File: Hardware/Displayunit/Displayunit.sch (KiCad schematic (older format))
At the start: 142 parts, among them IC1 TSC2007, IC2 MX25LM51245GXDI00, IC3 IS66WVH8M8BLL-100B1LI_0, IC4 TPS61165DRVR, J1 615008138221, J10 ER-CON10HT-1, J2 615008138221, J3 54104-4031, J4 Conn_ARM_JTAG_SWD_20, J5 52271-0679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

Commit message: Display Unit Zusätzliche Buchsen Mini Fit für den Bus, Befestigung um 5mm verschoben, Bauteil Placement.
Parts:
- removed C52: 5n6, Capacitor_SMD:C_0603_1608Metric, symbol Displayunit-rescue:C-Device
- removed J7: WAGO_Klemmleiste_2-pol, WAGO:WAGO_Klemmleiste_Hebel4mm²Horizontal_RM5mm_2-pol, symbol WAGO:WAGO_Klemmleiste_2-pol
- removed U6: SN65HVD231DR, Package_SO:SOIC-8_3.9x4.9mm_P1.27mm, symbol Interface_CAN_LIN:SN65HVD231
- added J11, J7: Conn_02x03_Row_Letter_First, Connector_Molex:Molex_Micro-Fit_3.0_43045-0612_2x03_P3.00mm_Vertical, symbol Connector_Generic:Conn_02x03_Row_Letter_First
- added R27, R28: 4k7, Resistor_SMD:R_0603_1608Metric, symbol Displayunit-rescue:R-Device
- added SW3, SW4: SW_DIP_x01, Button_Switch_SMD:SW_SPST_CK_RS282G05A3, symbol Switch:SW_DIP_x01
- added U6: SN65HVD234, Package_SO:SOIC-8_3.9x4.9mm_P1.27mm, symbol Interface_CAN_LIN:SN65HVD234
- R18: value 60R -> 120R
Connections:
- net +3V3: now also U6.3 (VCC)
- net CAN_STB: now also U6.8 (Rs)
- net GND: now also J11.b1 (Pin_b1), J7.b1 (Pin_b1), R27.2, R28.2, U6.2 (GND)
- net I2C2_SCL: now also R27.1
- net I2C2_SDA: now also R28.1
- net VrefCAN: no longer R18.2, R19.1
- net at D5.1 (A1), FB4.2: now also SW4.2, U6.6 (CANL); no longer R19.2
- net at D5.2 (A2), FB3.2, R18.1: now also U6.7 (CANH)
- net at R23.1, R6.1: now also U6.1 (D)
- net at R24.1, R25.1: now also U6.4 (R)
- net Control+2: now reaches C53.1, D2.2 (A)
- net Control+2: now also J11.a1 (Pin_a1), J7.a1 (Pin_a1)
- net CAN_EN: now reaches U1.72 (PB15)
- net CAN_EN: now also U6.5 (EN)
- net at FB12.1, J1.3, J2.3: now also J11.a2 (Pin_a2), J7.a2 (Pin_a2)
- net at FB3.1, J1.4, J2.4: now also J11.b2 (Pin_b2), J7.b2 (Pin_b2)
- net at FB4.1, J1.5, J2.5: now also J11.b3 (Pin_b3), J7.b3 (Pin_b3)
- net at FB11.1, J1.6, J2.6: now also J11.a3 (Pin_a3), J7.a3 (Pin_a3)
- net at D8.1 (A1), FB12.2, U3.6 (A): now also SW3.2; no longer R26.2
- new net: R18.2, SW4.1
- new net: R26.2, SW3.1
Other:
- moved on the sheet: J6, R18, R19, R23, R24, R25, R26, R6

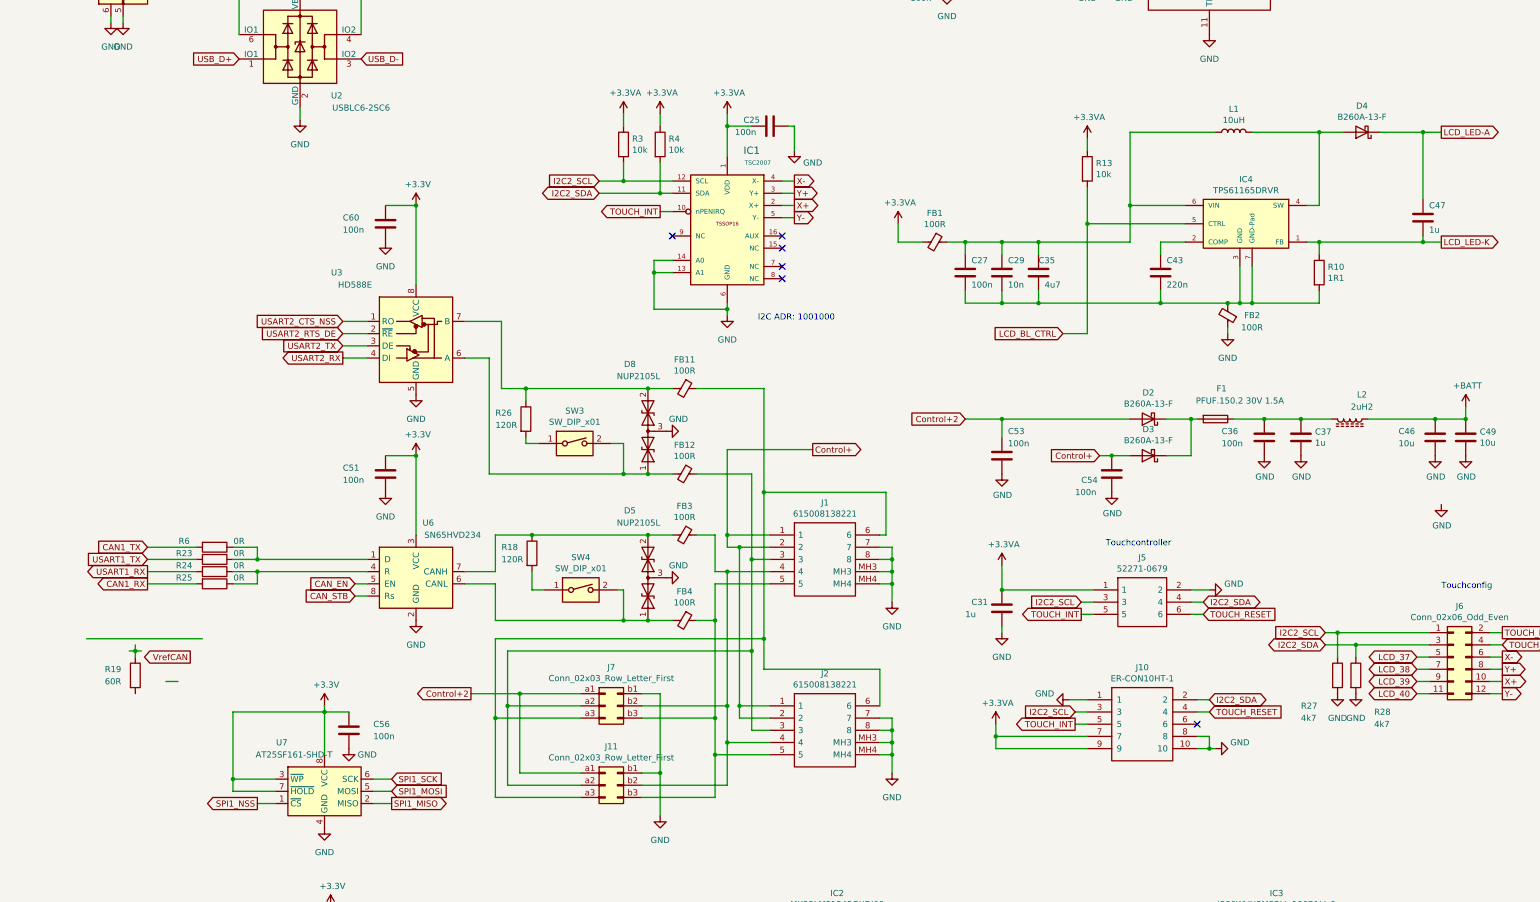
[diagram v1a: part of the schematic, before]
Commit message: Fehlende Teile gerouted
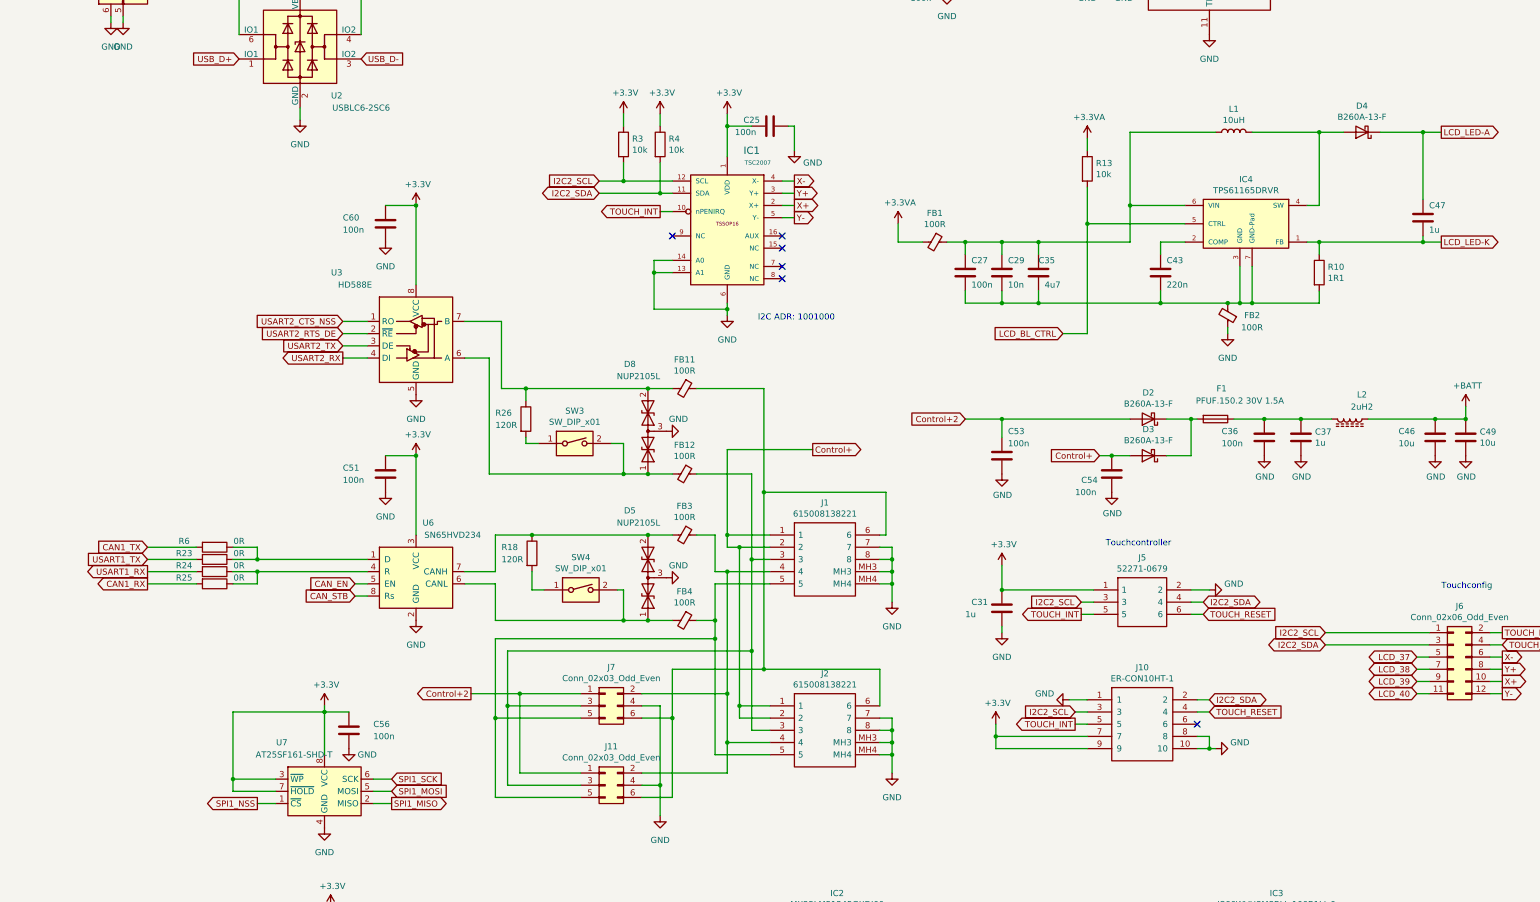
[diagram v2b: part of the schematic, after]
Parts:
- removed J11, J7: Conn_02x03_Row_Letter_First, Connector_Molex:Molex_Micro-Fit_3.0_43045-0612_2x03_P3.00mm_Vertical, symbol Connector_Generic:Conn_02x03_Row_Letter_First
- removed R19: 60R, Resistor_SMD:R_0603_1608Metric, symbol Displayunit-rescue:R-Device
- removed R27, R28: 4k7, Resistor_SMD:R_0603_1608Metric, symbol Displayunit-rescue:R-Device
- added J11, J7: Conn_02x03_Odd_Even, Connector_Molex:Molex_Micro-Fit_3.0_43045-0612_2x03_P3.00mm_Vertical, symbol Connector_Generic:Conn_02x03_Odd_Even
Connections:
- net +3.3VA: no longer C25.2, C31.1, IC1.1 (VDD), J10.7, J10.9, J5.1, R3.1, R4.1
- net +3V3: now also C25.2, C31.1, IC1.1 (VDD), J10.7, J10.9, J5.1, R3.1, R4.1
- net Control+2: now also J11.1 (Pin_1), J7.1 (Pin_1)
- net GND: now also J11.4 (Pin_4), J7.4 (Pin_4)
- net at FB12.1, J1.3, J2.3: now also J11.3 (Pin_3), J7.3 (Pin_3)
- net at FB3.1, J1.4, J2.4: now also J11.2 (Pin_2), J7.2 (Pin_2)
- net at FB4.1, J1.5, J2.5: now also J11.5 (Pin_5), J7.5 (Pin_5)
- net at FB11.1, J1.6, J2.6: now also J11.6 (Pin_6), J7.6 (Pin_6)
